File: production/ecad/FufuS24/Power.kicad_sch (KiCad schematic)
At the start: 58 parts, among them J7 691137710002, U4 TPS785, U5 PLMR38020FDDAR, U6 PLMR38020FDDAR, U7 PLMR38020FDDAR

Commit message: Big layout push
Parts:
- C1, C27, C32, C34: footprint footprints:CAPC2012X94N -> Capacitor_SMD:C_1210_3225Metric
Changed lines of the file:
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@@
   (junction (at 162.56 152.4) (diameter 0) (color 0 0 0 0)
   )
+  (junction (at 205.74 31.75) (diameter 0) (color 0 0 0 0)
+  )
   (junction (at 246.38 31.75) (diameter 0) (color 0 0 0 0)
   )
@@
   (junction (at 48.26 144.78) (diameter 0) (color 0 0 0 0)
   )
-  (junction (at 205.74 31.75) (diameter 0) (color 0 0 0 0)
-  )
   (junction (at 162.56 93.98) (diameter 0) (color 0 0 0 0)
   )
@@
     )
   )
-  (symbol (lib_id "Device:C") (at 205.74 35.56 0) (unit 1)
-    (in_bom yes) (on_board yes) (dnp no)
-    (property "Reference" "C34" (at 209.55 34.29 0)
-      (effects (font (size 1.27 1.27)) (justify left))
-    )
-    (property "Value" "4.7uF" (at 209.55 36.83 0)
-      (effects (font (size 1.27 1.27)) (justify left))
-    )
-    (property "Footprint" "footprints:CAPC2012X94N" (at 206.7052 39.37 0)
-      (effects (font (size 1.27 1.27)) hide)
-    )
-    (property "Datasheet" "~" (at 205.74 35.56 0)
-      (effects (font (size 1.27 1.27)) hide)
-    )
-    (property "Voltage" "100V" (at 209.55 39.37 0)
-      (effects (font (size 1.27 1.27)) (justify left))
-    )
-    (property "MPN" "KAM32LR72A475KU" (at 205.74 35.56 0)
-      (effects (font (size 1.27 1.27)) hide)
-    )
-    (pin "1")
-    (pin "2")
-    (instances
-      (project "FufuS24"
-        (path "/c4c3980b-c8c0-435e-abdc-bbed2349d7ac/1f62379a-1fa8-439b-93cd-7c736b3b1bba"
-          (reference "C34") (unit 1)
-        )
-      )
-    )
-  )
   (symbol (lib_id "CL21A106KAYNNNG:CL21A106KAYNNNG") (at 149.86 163.83 270) (unit 1)
     (in_bom yes) (on_board yes) (dnp no)
@@
     )
   )
-  (symbol (lib_id "Device:C") (at 20.32 163.83 0) (unit 1)
-    (in_bom yes) (on_board yes) (dnp no)
-    (property "Reference" "C1" (at 24.13 162.56 0)
-      (effects (font (size 1.27 1.27)) (justify left))
-    )
-    (property "Value" "4.7uF" (at 24.13 165.1 0)
-      (effects (font (size 1.27 1.27)) (justify left))
-    )
-    (property "Footprint" "footprints:CAPC2012X94N" (at 21.2852 167.64 0)
-      (effects (font (size 1.27 1.27)) hide)
-    )
-    (property "Datasheet" "~" (at 20.32 163.83 0)
-      (effects (font (size 1.27 1.27)) hide)
-    )
-    (property "Voltage" "100V" (at 24.13 167.64 0)
-      (effects (font (size 1.27 1.27)) (justify left))
-    )
-    (property "MPN" "KAM32LR72A475KU" (at 20.32 163.83 0)
-      (effects (font (size 1.27 1.27)) hide)
-    )
-    (pin "1")
-    (pin "2")
-    (instances
-      (project "FufuS24"
-        (path "/c4c3980b-c8c0-435e-abdc-bbed2349d7ac/1f62379a-1fa8-439b-93cd-7c736b3b1bba"
-          (reference "C1") (unit 1)
-        )
-      )
-    )
-  )
   (symbol (lib_id "power:+3V3") (at 276.86 130.81 0) (unit 1)
     (in_bom yes) (on_board yes) (dnp no) (fields_autoplaced)
@@
     )
   )
+  (symbol (lib_id "Device:C") (at 20.32 163.83 0) (unit 1)
+    (in_bom yes) (on_board yes) (dnp no)
+    (property "Reference" "C1" (at 24.13 162.56 0)
+      (effects (font (size 1.27 1.27)) (justify left))
+    )
+    (property "Value" "4.7uF" (at 24.13 165.1 0)
+      (effects (font (size 1.27 1.27)) (justify left))
+    )
+    (property "Footprint" "Capacitor_SMD:C_1210_3225Metric" (at 21.2852 167.64 0)
+      (effects (font (size 1.27 1.27)) hide)
+    )
+    (property "Datasheet" "~" (at 20.32 163.83 0)
+      (effects (font (size 1.27 1.27)) hide)
+    )
+    (property "Voltage" "100V" (at 24.13 167.64 0)
+      (effects (font (size 1.27 1.27)) (justify left))
+    )
+    (property "MPN" "KAM32LR72A475KU" (at 20.32 163.83 0)
+      (effects (font (size 1.27 1.27)) hide)
+    )
+    (pin "1")
+    (pin "2")
+    (instances
+      (project "FufuS24"
+        (path "/c4c3980b-c8c0-435e-abdc-bbed2349d7ac/1f62379a-1fa8-439b-93cd-7c736b3b1bba"
+          (reference "C1") (unit 1)
+        )
+      )
+    )
+  )
   (symbol (lib_id "5014:5014") (at 252.73 133.35 180) (unit 1)
     (in_bom yes) (on_board yes) (dnp no) (fields_autoplaced)
@@
     )
   )
+  (symbol (lib_id "Device:C") (at 205.74 35.56 0) (unit 1)
+    (in_bom yes) (on_board yes) (dnp no)
+    (property "Reference" "C34" (at 209.55 34.29 0)
+      (effects (font (size 1.27 1.27)) (justify left))
+    )
+    (property "Value" "4.7uF" (at 209.55 36.83 0)
+      (effects (font (size 1.27 1.27)) (justify left))
+    )
+    (property "Footprint" "Capacitor_SMD:C_1210_3225Metric" (at 206.7052 39.37 0)
+      (effects (font (size 1.27 1.27)) hide)
+    )
+    (property "Datasheet" "~" (at 205.74 35.56 0)
+      (effects (font (size 1.27 1.27)) hide)
+    )
+    (property "Voltage" "100V" (at 209.55 39.37 0)
+      (effects (font (size 1.27 1.27)) (justify left))
+    )
+    (property "MPN" "KAM32LR72A475KU" (at 205.74 35.56 0)
+      (effects (font (size 1.27 1.27)) hide)
+    )
+    (pin "1")
+    (pin "2")
+    (instances
+      (project "FufuS24"
+        (path "/c4c3980b-c8c0-435e-abdc-bbed2349d7ac/1f62379a-1fa8-439b-93cd-7c736b3b1bba"
+          (reference "C34") (unit 1)
+        )
+      )
+    )
+  )
   (symbol (lib_id "CL21A106KAYNNNG:CL21A106KAYNNNG") (at 246.38 31.75 270) (unit 1)
     (in_bom yes) (on_board yes) (dnp no) (fields_autoplaced)
@@
     )
   )
-  (symbol (lib_id "Device:C") (at 19.05 35.56 0) (unit 1)
-    (in_bom yes) (on_board yes) (dnp no)
-    (property "Reference" "C27" (at 22.86 34.29 0)
-      (effects (font (size 1.27 1.27)) (justify left))
-    )
-    (property "Value" "4.7uF" (at 22.86 36.83 0)
-      (effects (font (size 1.27 1.27)) (justify left))
-    )
-    (property "Footprint" "footprints:CAPC2012X94N" (at 20.0152 39.37 0)
-      (effects (font (size 1.27 1.27)) hide)
-    )
-    (property "Datasheet" "~" (at 19.05 35.56 0)
-      (effects (font (size 1.27 1.27)) hide)
-    )
-    (property "Voltage" "100V" (at 22.86 39.37 0)
-      (effects (font (size 1.27 1.27)) (justify left))
-    )
-    (property "MPN" "KAM32LR72A475KU" (at 19.05 35.56 0)
-      (effects (font (size 1.27 1.27)) hide)
-    )
-    (pin "1")
-    (pin "2")
-    (instances
-      (project "FufuS24"
-        (path "/c4c3980b-c8c0-435e-abdc-bbed2349d7ac/1f62379a-1fa8-439b-93cd-7c736b3b1bba"
-          (reference "C27") (unit 1)
-        )
-      )
-    )
-  )
   (symbol (lib_id "150080GS75000:150080GS75000") (at 217.17 144.78 270) (unit 1)
     (in_bom yes) (on_board yes) (dnp no) (fields_autoplaced)
@@
       (effects (font (size 1.27 1.27)) (justify left))
     )
-    (property "Footprint" "footprints:CAPC2012X94N" (at 21.2852 109.22 0)
+    (property "Footprint" "Capacitor_SMD:C_1210_3225Metric" (at 21.2852 109.22 0)
       (effects (font (size 1.27 1.27)) hide)
     )
@@
         )
       )
+    )
+  )
+  (symbol (lib_id "Device:C") (at 19.05 35.56 0) (unit 1)
+    (in_bom yes) (on_board yes) (dnp no)
+    (property "Reference" "C27" (at 22.86 34.29 0)
+      (effects (font (size 1.27 1.27)) (justify left))
+    )
+    (property "Value" "4.7uF" (at 22.86 36.83 0)
+      (effects (font (size 1.27 1.27)) (justify left))
+    )
+    (property "Footprint" "Capacitor_SMD:C_1210_3225Metric" (at 20.0152 39.37 0)
+      (effects (font (size 1.27 1.27)) hide)
+    )
+    (property "Datasheet" "~" (at 19.05 35.56 0)
+      (effects (font (size 1.27 1.27)) hide)
+    )
+    (property "Voltage" "100V" (at 22.86 39.37 0)
+      (effects (font (size 1.27 1.27)) (justify left))
+    )
+    (property "MPN" "KAM32LR72A475KU" (at 19.05 35.56 0)
+      (effects (font (size 1.27 1.27)) hide)
+    )
+    (pin "1")
+    (pin "2")
+    (instances
+      (project "FufuS24"
+        (path "/c4c3980b-c8c0-435e-abdc-bbed2349d7ac/1f62379a-1fa8-439b-93cd-7c736b3b1bba"
+          (reference "C27") (unit 1)
+        )
+      )

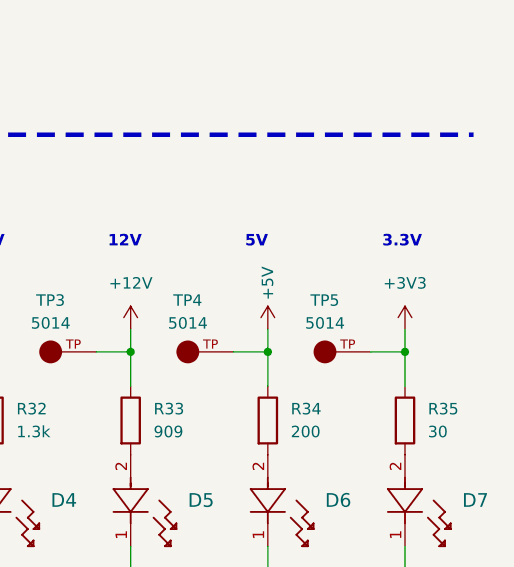
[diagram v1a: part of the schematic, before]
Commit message: major layout changes
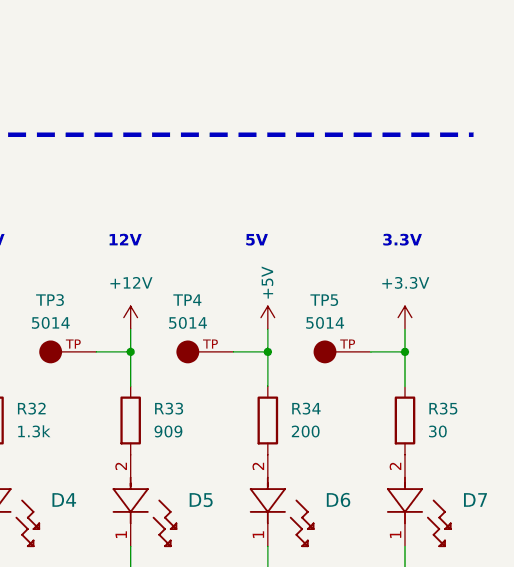
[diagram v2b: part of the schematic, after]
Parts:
- U5, U6, U7: footprint footprints:DDA0008E-MFG -> footprints:DDA0008E-IPC_A
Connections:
- net +3V3 is gone; now on net +3.3V: R35.1, TP5.TP
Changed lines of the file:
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@@
+    )
+  )
+  (symbol (lib_id "power:+3.3V") (at 276.86 130.81 0) (unit 1)
+    (in_bom yes) (on_board yes) (dnp no) (fields_autoplaced)
+    (property "Reference" "#PWR050" (at 276.86 134.62 0)
+      (effects (font (size 1.27 1.27)) hide)
+    )
+    (property "Value" "+3.3V" (at 276.86 125.73 0)
+      (effects (font (size 1.27 1.27)))
+    )
+    (property "Footprint" "" (at 276.86 130.81 0)
+      (effects (font (size 1.27 1.27)) hide)
+    )
+    (property "Datasheet" "" (at 276.86 130.81 0)
+      (effects (font (size 1.27 1.27)) hide)
+    )
+    (pin "1")
+    (instances
+      (project "FufuS24"
+        (path "/c4c3980b-c8c0-435e-abdc-bbed2349d7ac/1f62379a-1fa8-439b-93cd-7c736b3b1bba"
+          (reference "#PWR050") (unit 1)
+        )
+      )
     )
   )
@@
     )
   )
-  (symbol (lib_id "power:+3V3") (at 276.86 130.81 0) (unit 1)
-    (in_bom yes) (on_board yes) (dnp no) (fields_autoplaced)
-    (property "Reference" "#PWR050" (at 276.86 134.62 0)
-      (effects (font (size 1.27 1.27)) hide)
-    )
-    (property "Value" "+3V3" (at 276.86 125.73 0)
-      (effects (font (size 1.27 1.27)))
-    )
-    (property "Footprint" "" (at 276.86 130.81 0)
-      (effects (font (size 1.27 1.27)) hide)
-    )
-    (property "Datasheet" "" (at 276.86 130.81 0)
-      (effects (font (size 1.27 1.27)) hide)
-    )
-    (pin "1")
-    (instances
-      (project "FufuS24"
-        (path "/c4c3980b-c8c0-435e-abdc-bbed2349d7ac/1f62379a-1fa8-439b-93cd-7c736b3b1bba"
-          (reference "#PWR050") (unit 1)
-        )
-      )
-    )
-  )
   (symbol (lib_id "power:GNDREF") (at 46.99 184.15 0) (unit 1)
     (in_bom yes) (on_board yes) (dnp no) (fields_autoplaced)
@@
       (effects (font (size 1.524 1.524)))
     )
-    (property "Footprint" "footprints:DDA0008E-MFG" (at 45.72 139.7 0)
+    (property "Footprint" "footprints:DDA0008E-IPC_A" (at 45.72 139.7 0)
       (effects (font (size 1.27 1.27) italic) hide)
     )
@@
       (effects (font (size 1.524 1.524)))
     )
-    (property "Footprint" "footprints:DDA0008E-MFG" (at 45.72 81.28 0)
+    (property "Footprint" "footprints:DDA0008E-IPC_A" (at 45.72 81.28 0)
       (effects (font (size 1.27 1.27) italic) hide)
     )
@@
       (effects (font (size 1.524 1.524)))
     )
-    (property "Footprint" "footprints:DDA0008E-MFG" (at 45.72 20.32 0)
-      (effects (font (size 1.27 1.27) italic) hide)
-    )
+    (property "Footprint" "footprints:DDA0008E-IPC_A" (at 45.72 20.32 0)
+      (effects (font (size 1.27 1.27) italic) hide)
+    )

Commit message: revised high speed signals
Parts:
- added TP17 (x3): 5014, footprints:TP_5014, symbol 5014:5014
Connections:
- net GNDREF: now also TP17.TP, TP17.TP, TP17.TP

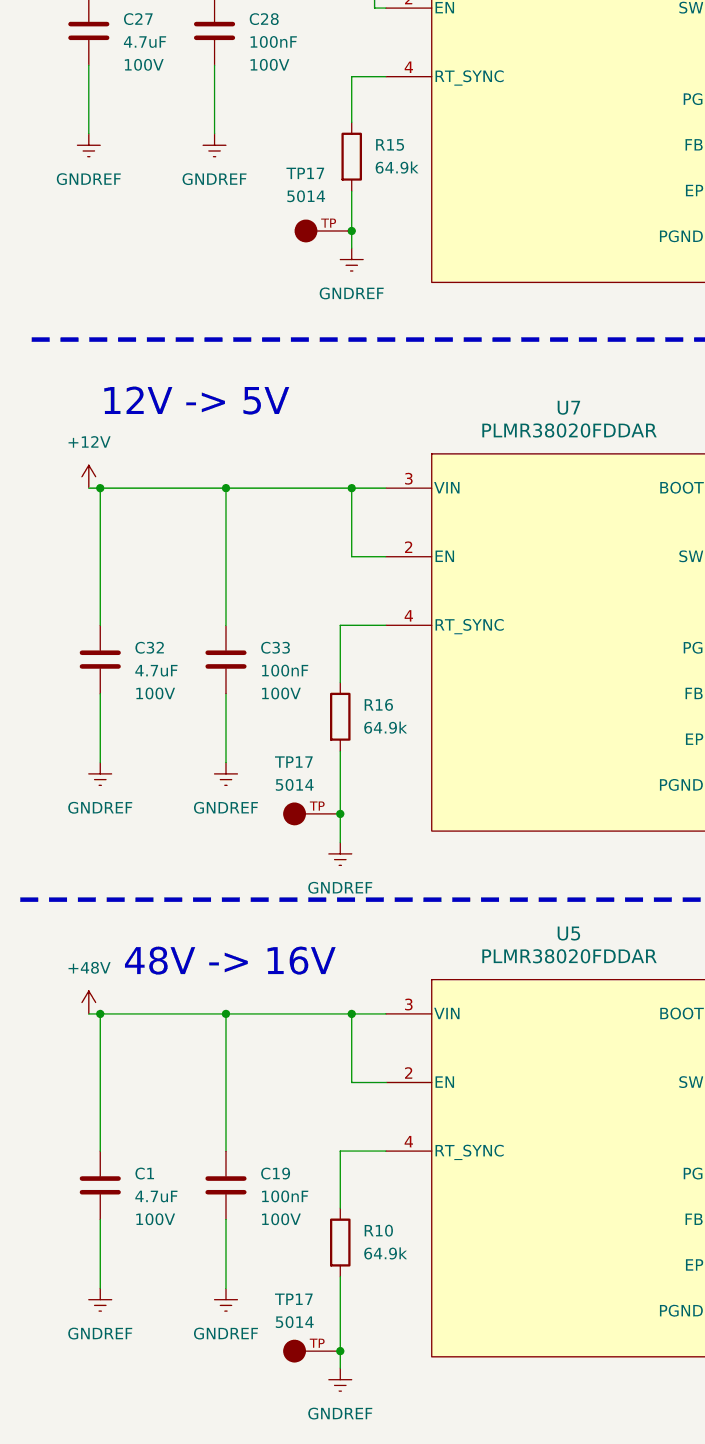
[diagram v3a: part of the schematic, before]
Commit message: updated water sensor
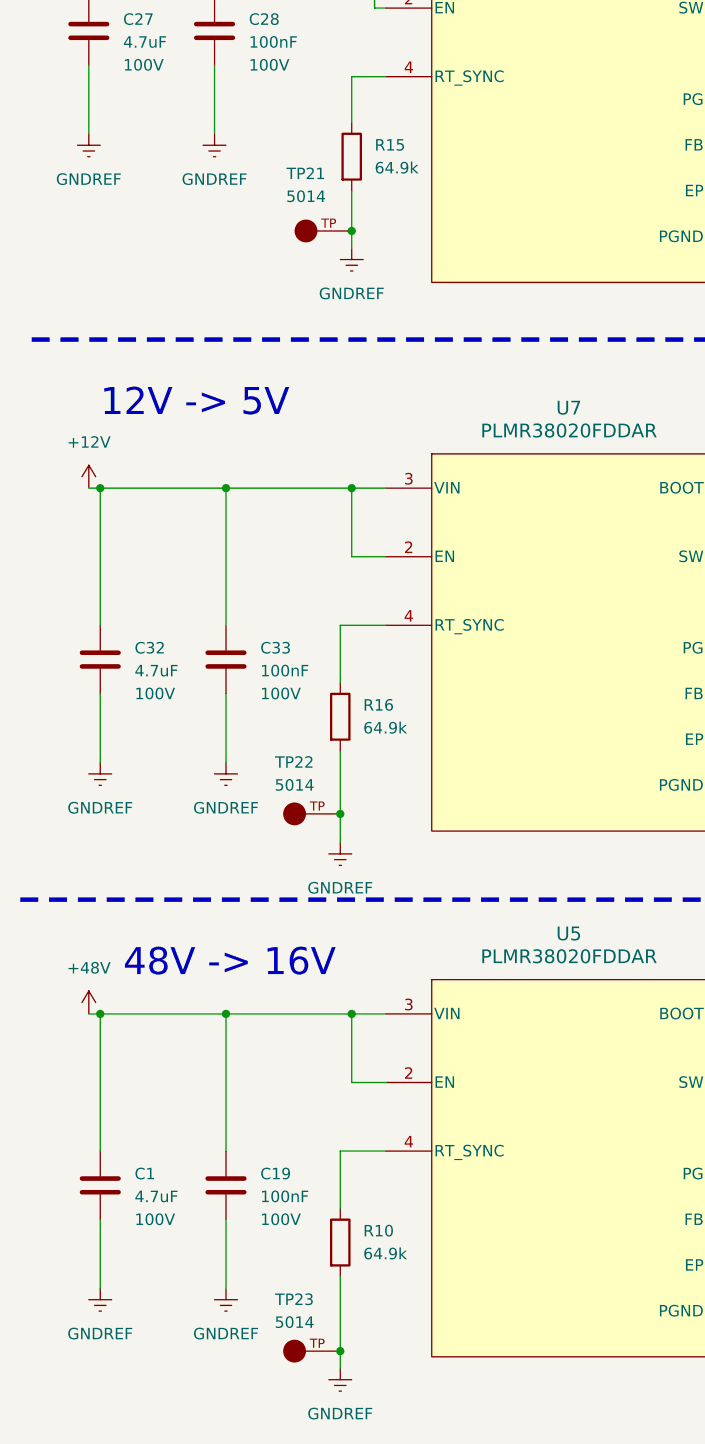
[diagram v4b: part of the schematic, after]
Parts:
- renumbered TP17 to TP21, TP17 to TP22, TP17 to TP23
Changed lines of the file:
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@@
   (symbol (lib_id "5014:5014") (at 41.91 122.555 180) (unit 1)
     (in_bom yes) (on_board yes) (dnp no) (fields_autoplaced)
-    (property "Reference" "TP17" (at 41.91 116.84 0)
+    (property "Reference" "TP22" (at 41.91 116.84 0)
       (effects (font (size 1.27 1.27)))
     )
@@
     (instances
       (project "FufuS24"
-        (path "/c4c3980b-c8c0-435e-abdc-bbed2349d7ac/57fb5dcd-e779-40d3-8741-57c7eee1ca58"
-          (reference "TP17") (unit 1)
-        )
         (path "/c4c3980b-c8c0-435e-abdc-bbed2349d7ac/1f62379a-1fa8-439b-93cd-7c736b3b1bba"
           (reference "TP22") (unit 1)
@@
   (symbol (lib_id "5014:5014") (at 43.18 57.785 180) (unit 1)
     (in_bom yes) (on_board yes) (dnp no) (fields_autoplaced)
-    (property "Reference" "TP17" (at 43.18 51.435 0)
+    (property "Reference" "TP21" (at 43.18 51.435 0)
       (effects (font (size 1.27 1.27)))
     )
@@
     (instances
       (project "FufuS24"
-        (path "/c4c3980b-c8c0-435e-abdc-bbed2349d7ac/57fb5dcd-e779-40d3-8741-57c7eee1ca58"
-          (reference "TP17") (unit 1)
-        )
         (path "/c4c3980b-c8c0-435e-abdc-bbed2349d7ac/1f62379a-1fa8-439b-93cd-7c736b3b1bba"
           (reference "TP21") (unit 1)
@@
   (symbol (lib_id "5014:5014") (at 41.91 182.245 180) (unit 1)
     (in_bom yes) (on_board yes) (dnp no) (fields_autoplaced)
-    (property "Reference" "TP17" (at 41.91 176.53 0)
+    (property "Reference" "TP23" (at 41.91 176.53 0)
       (effects (font (size 1.27 1.27)))
     )
@@
     (instances
       (project "FufuS24"
-        (path "/c4c3980b-c8c0-435e-abdc-bbed2349d7ac/57fb5dcd-e779-40d3-8741-57c7eee1ca58"
-          (reference "TP17") (unit 1)
-        )
         (path "/c4c3980b-c8c0-435e-abdc-bbed2349d7ac/1f62379a-1fa8-439b-93cd-7c736b3b1bba"
           (reference "TP23") (unit 1)

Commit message: fixed some DRC
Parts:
- U5, U6, U7: footprint footprints:DDA0008E-IPC_A -> footprints:DDA0008E-IPC_B
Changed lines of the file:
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@@
       (effects (font (size 1.524 1.524)))
     )
-    (property "Footprint" "footprints:DDA0008E-IPC_A" (at 45.72 139.7 0)
+    (property "Footprint" "footprints:DDA0008E-IPC_B" (at 45.72 139.7 0)
       (effects (font (size 1.27 1.27) italic) hide)
     )
@@
       (effects (font (size 1.524 1.524)))
     )
-    (property "Footprint" "footprints:DDA0008E-IPC_A" (at 45.72 81.28 0)
+    (property "Footprint" "footprints:DDA0008E-IPC_B" (at 45.72 81.28 0)
       (effects (font (size 1.27 1.27) italic) hide)
     )
@@
       (effects (font (size 1.524 1.524)))
     )
-    (property "Footprint" "footprints:DDA0008E-IPC_A" (at 45.72 20.32 0)
-      (effects (font (size 1.27 1.27) italic) hide)
-    )
+    (property "Footprint" "footprints:DDA0008E-IPC_B" (at 45.72 20.32 0)
+      (effects (font (size 1.27 1.27) italic) hide)
+    )
